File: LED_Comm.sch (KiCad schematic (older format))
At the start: 23 parts

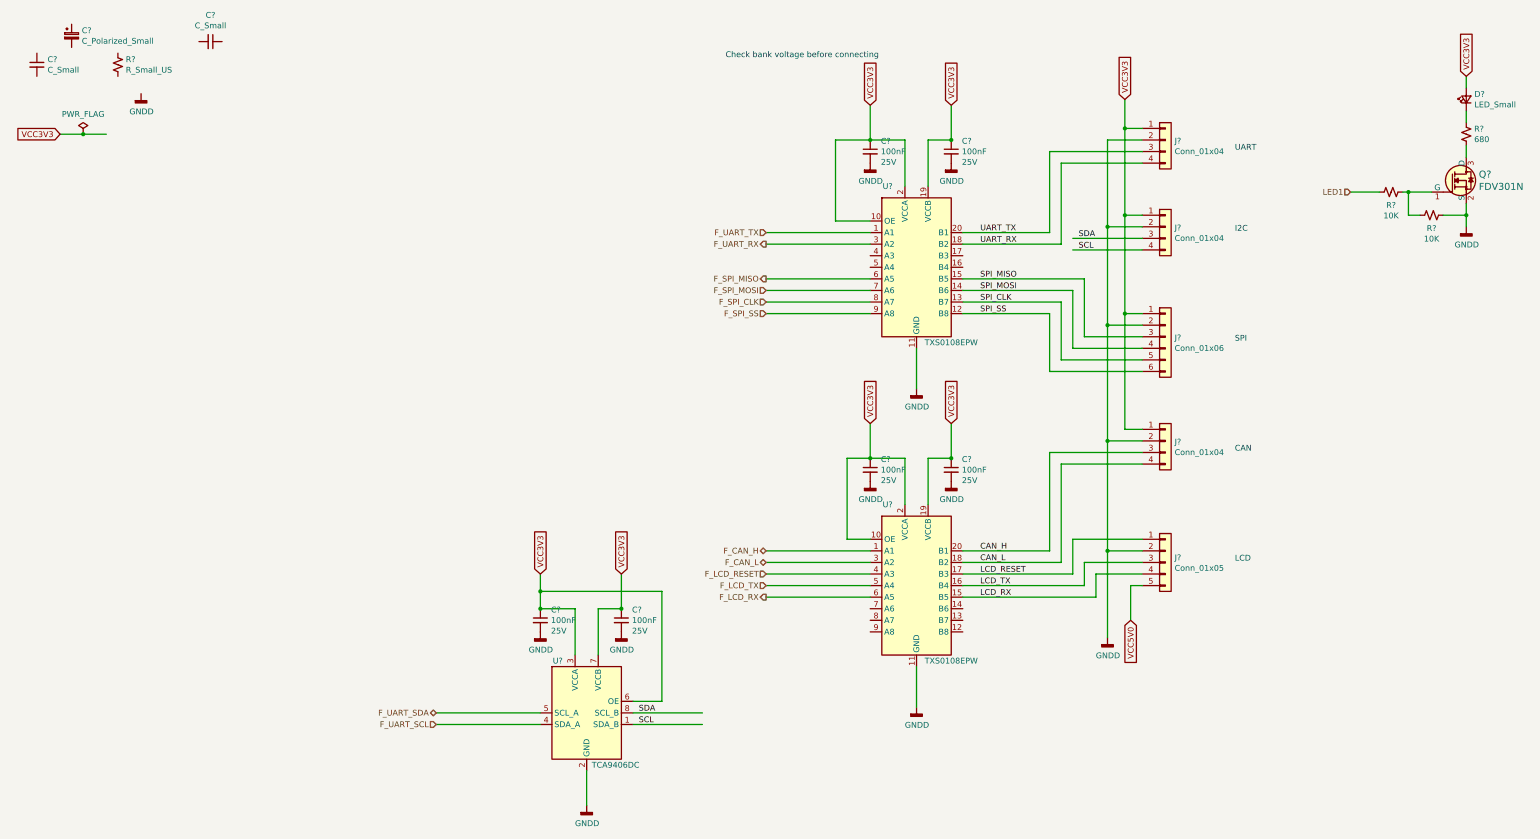
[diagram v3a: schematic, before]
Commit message: PCB created and schematics annotated High speed connections added to the BTB
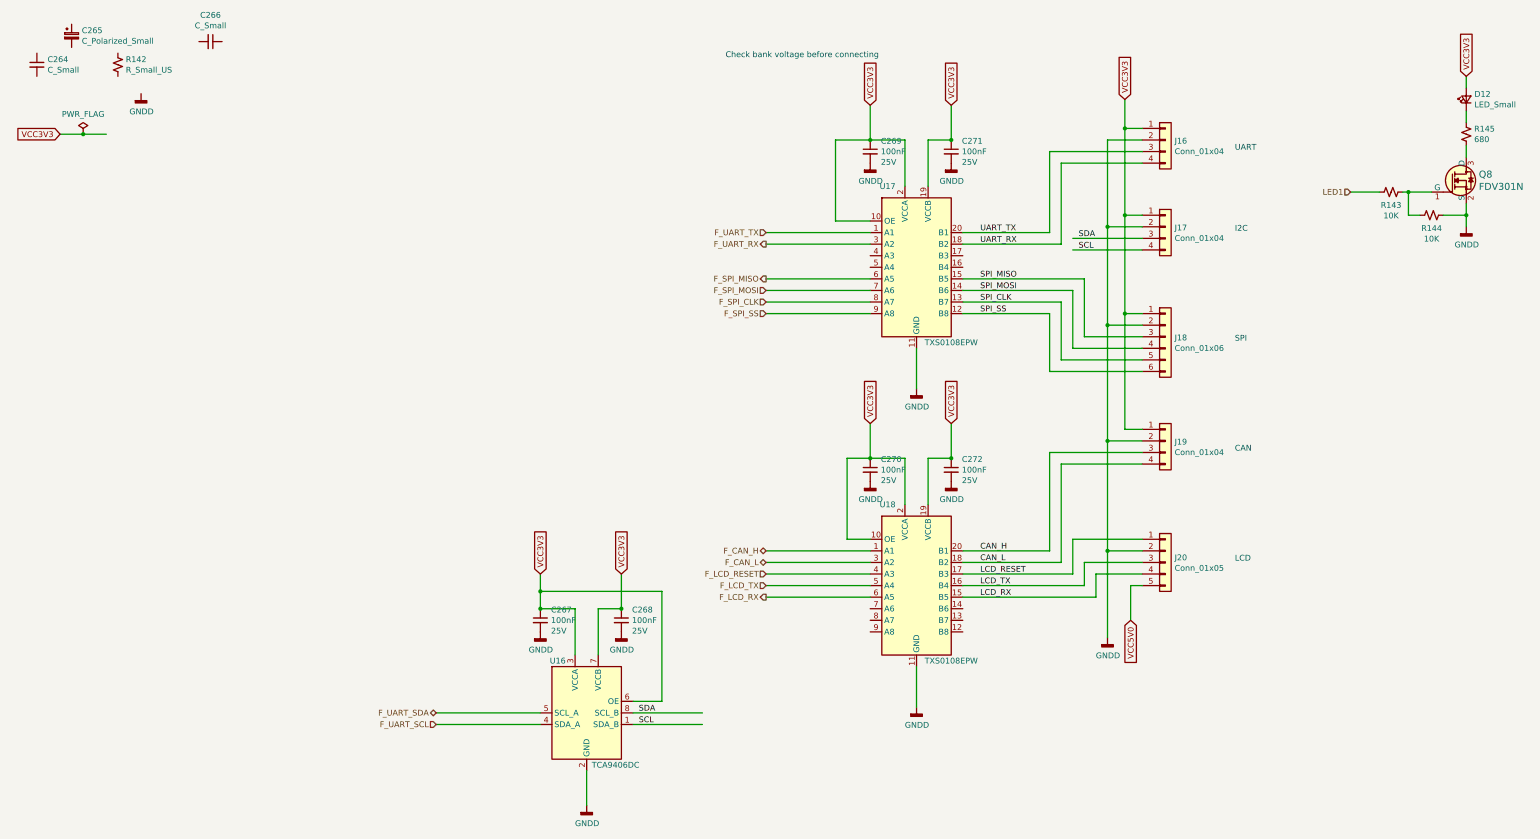
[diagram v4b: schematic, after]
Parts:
- gave numbers to parts that had none: 23

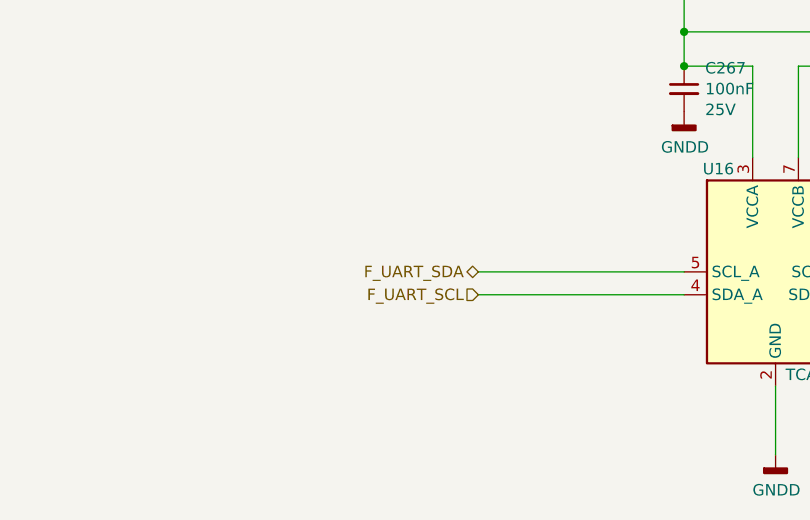
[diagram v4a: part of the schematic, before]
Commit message: Connections were made to FPGA banks
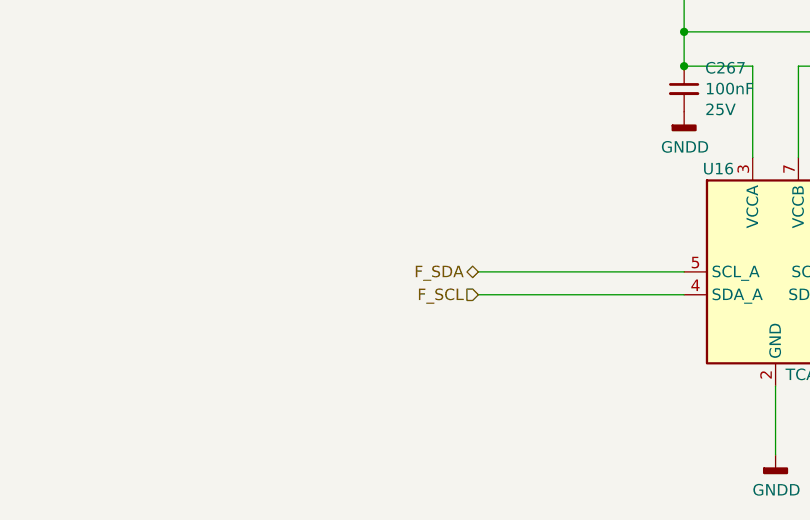
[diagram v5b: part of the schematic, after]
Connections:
- net labels added: F_SCL, F_SDA
- net labels removed: F_UART_SCL, F_UART_SDA
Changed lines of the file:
@@
 $Descr A4 11693 8268
 encoding utf-8
-Sheet 17 25
+Sheet 15 25
 Title "CGMPCX1006"
 Date "2021-02-03"
@@
 F_UART_RX
 Text HLabel 1200 6800 0    50   BiDi ~ 0
-F_UART_SDA
+F_SDA
 Text HLabel 1200 6900 0    50   Input ~ 0
-F_UART_SCL
+F_SCL
 Wire Wire Line
 	4950 2550 4650 2550

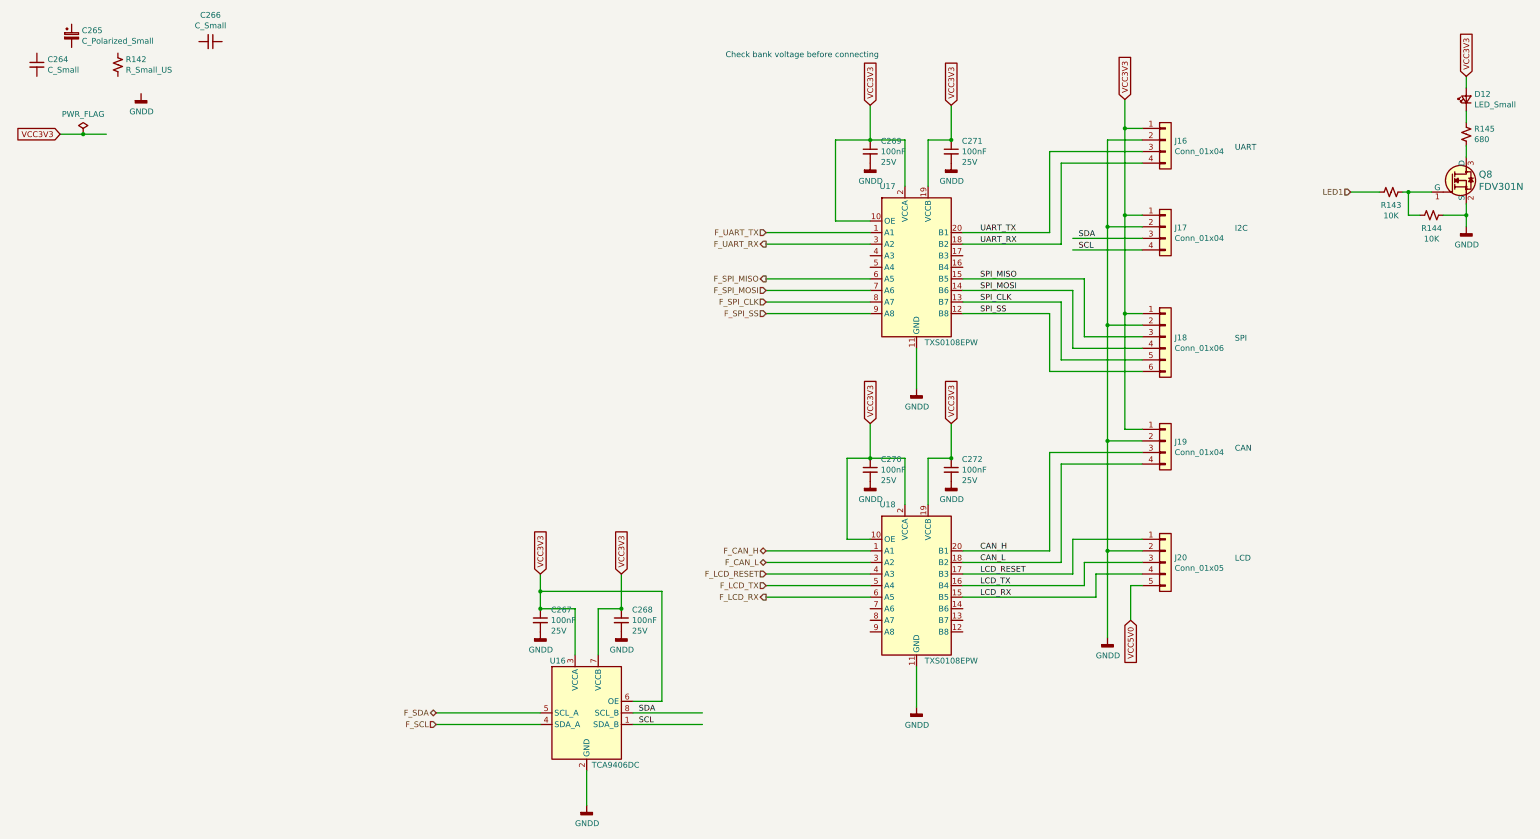
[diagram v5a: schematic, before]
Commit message: Corrected PCB import errors
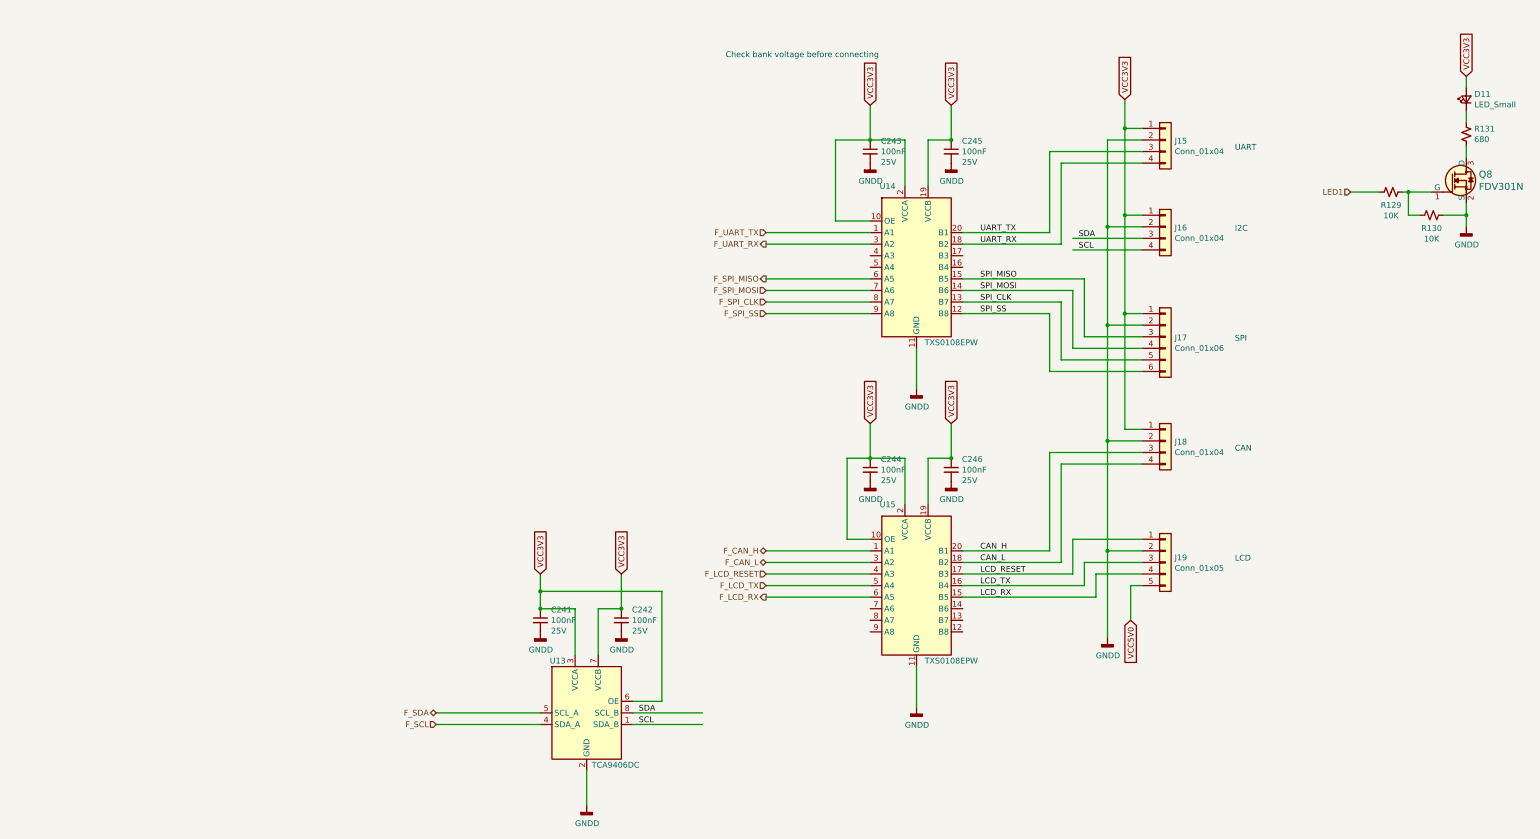
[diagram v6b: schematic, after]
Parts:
- removed C264: C_Small, Capacitor_SMD:C_0603_1608Metric_Pad1.08x0.95mm_HandSolder, symbol Device:C_Small
- removed C265: C_Polarized_Small, Capacitor_Tantalum_SMD:CP_EIA-1608-10_AVX-L_Pad1.25x1.05mm_HandSolder, symbol Device:C_Polarized_Small
- removed C266: C_Small, symbol Device:C_Small
- removed R142: R_Small_US, Resistor_SMD:R_0603_1608Metric_Pad0.98x0.95mm_HandSolder, symbol Device:R_Small_US
- D11: renamed from D12; footprint (none) -> LED_SMD:LED_0603_1608Metric
- J15: renamed from J16; footprint (none) -> Connector_PinHeader_2.54mm:PinHeader_1x04_P2.54mm_Vertical
- J16: renamed from J17; footprint (none) -> Connector_PinHeader_2.54mm:PinHeader_1x04_P2.54mm_Vertical
- J17: renamed from J18; footprint (none) -> Connector_PinHeader_2.54mm:PinHeader_1x06_P2.54mm_Vertical
- J18: renamed from J19; footprint (none) -> Connector_PinHeader_2.54mm:PinHeader_1x04_P2.54mm_Vertical
- J19: renamed from J20; footprint (none) -> Connector_PinHeader_2.54mm:PinHeader_1x05_P2.54mm_Vertical
- renumbered C267 to C241, C268 to C242, C269 to C243, C270 to C244, C271 to C245, C272 to C246, R143 to R129, R144 to R130, R145 to R131, U16 to U13, U17 to U14, U18 to U15
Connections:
- wire segments 114 -> 112
